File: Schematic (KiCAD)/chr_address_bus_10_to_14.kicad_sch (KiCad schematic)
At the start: 80 parts

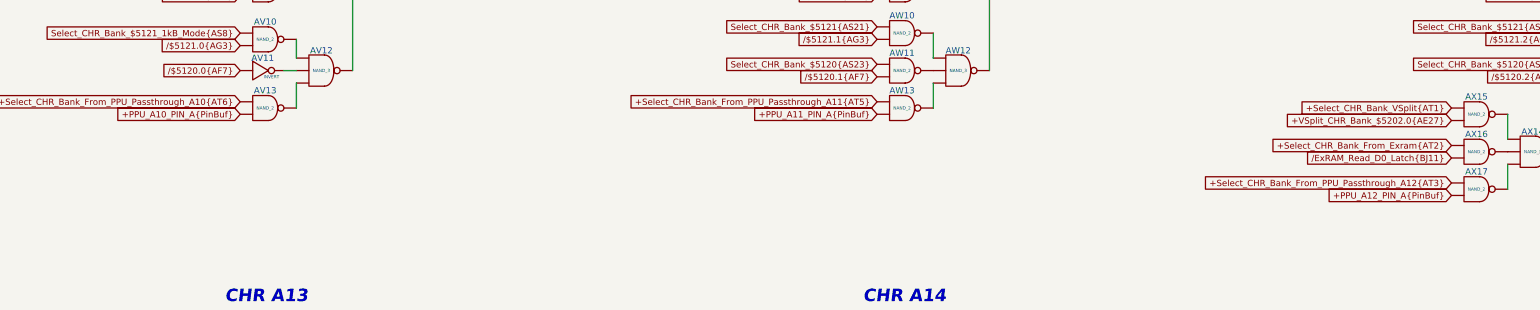
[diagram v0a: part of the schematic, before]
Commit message: Tracing and schematic updates.  - Added timer to schematic.  - Added all items from artifacts sheet to the MMC5A trace.
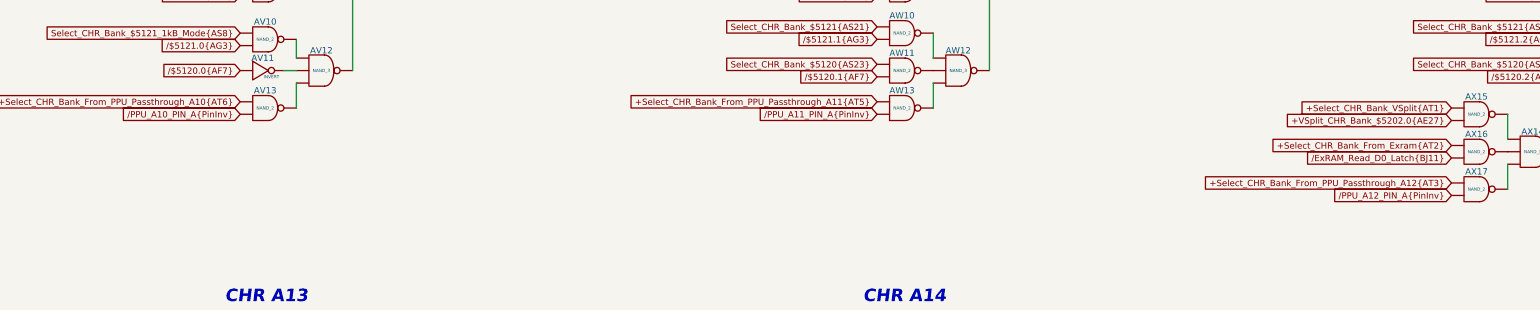
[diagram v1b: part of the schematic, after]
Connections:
- net +PPU_A10_PIN_A{PinBuf} is gone; now on net /PPU_A10_PIN_A{PinInv}: AV13. (X)
- net +PPU_A12_PIN_A{PinBuf} is gone; now on net /PPU_A12_PIN_A{PinInv}: AX17. (X)
- net at AX8. (X): now also AX6. (X); no longer AX7. (X)
- net at AV3. (X): now also AV4. (X); no longer AV1. (X)
- net at AW8. (X): now also AW6. (X); no longer AW5. (X)
- net at AW12. (X): now also AW11. (X); no longer AW13. (X)
- net at AX4. (X): now also AX2. (X); no longer AX9. (X)
- net at AZ14. (X): now also AZ13. (X); no longer AZ16. (X)
- net at AW9. (X): now also AW8. (X); no longer AW14. (X)
- net at AY8. (X): now also AY6. (X); no longer AY7. (X)
- net at AZ8. (X): now also AZ6. (X); no longer AZ5. (X)
- net at AY14. (X): now also AY13. (X); no longer AY15. (X)
- net at AY13. (X): now also AY12. (X); no longer AY14. (X)
- net at AX14. (X): now also AX17. (X); no longer AX16. (X)
- net at AX13. (X): now also AX12. (X); no longer AX14. (X)
- net /PPU_A12_PIN_A{PinInv}: now reaches AX17. (X)
- net /PPU_A12_PIN_A{PinInv}: no longer AX14. (X)
- net at AV9. (X): now also AV3. (X); no longer AV12. (X)
- net at AV8. (X): now also AV6. (X); no longer AV9. (X)
- net at AX12. (X): now also AX10. (X); no longer AX11. (X)
- net at AZ13. (X): now also AZ12. (X); no longer AZ14. (X)
- net at AX9. (X): now also AX18. (X); no longer AX12. (X)
- net at AY4. (X): now also AY9. (X); no longer AY1. (X)
- net at AZ4. (X): now also AZ2. (X); no longer AZ3. (X)
- net at AZ9. (X): now also AZ17. (X); no longer AZ4. (X)
- net at AY9. (X): now also AY17. (X); no longer AY4. (X)
- net at AV12. (X): now also AV13. (X); no longer AV10. (X)
- net /PPU_A10_PIN_A{PinInv}: now reaches AV13. (X)
- net /PPU_A10_PIN_A{PinInv}: no longer AV12. (X)
- net at AW4. (X): now also AW1. (X); no longer AW9. (X)
- net +PPU_A11_PIN_A{PinBuf} renamed /PPU_A11_PIN_A{PinInv}
- new net: AX7. (X), AX8. (X)
- new net: AV1. (X), AV3. (X)
- new net: AW5. (X), AW8. (X)
- new net: AW12. (X), AW13. (X)
- new net: AX4. (X), AX9. (X)
- new net: AX3. (X), AX4. (X)
- new net: AX1. (X), AX4. (X)
- new net: AZ14. (X), AZ16. (X)
- new net: AW14. (X), AW9. (X)
- new net: AY7. (X), AY8. (X)
- new net: AZ5. (X), AZ8. (X)
- new net: AW7. (X), AW8. (X)
- new net: AX5. (X), AX8. (X)
- new net: AY14. (X), AY15. (X)
- new net: AY14. (X), AY16. (X)
- new net: AX14. (X), AX16. (X)
- new net: AX13. (X), AX14. (X)
- new net: AX14. (X), AX15. (X)
- new net: AZ7. (X), AZ8. (X)
- new net: AV12. (X), AV9. (X)
- new net: AV8. (X), AV9. (X)
- new net: AV14. (X), AV9. (X)
- new net: AX11. (X), AX12. (X)
- new net: AZ14. (X), AZ15. (X)
- new net: AZ11. (X), AZ12. (X)
- new net: AX12. (X), AX9. (X)
- new net: AY1. (X), AY4. (X)
- new net: AZ3. (X), AZ4. (X)
- new net: AZ4. (X), AZ9. (X)
- new net: AZ1. (X), AZ4. (X)
- new net: AY3. (X), AY4. (X)
- new net: AY2. (X), AY4. (X)
- new net: AV10. (X), AV12. (X)
- new net: AV11. (X), AV12. (X)
- new net: AW12. (X), AW9. (X)
- new net: AW4. (X), AW9. (X)
- new net: AW10. (X), AW12. (X)
- new net: AX8. (X), AX9. (X)
- new net: AV7. (X), AV8. (X)
- new net: AY8. (X), AY9. (X)
- new net: AY5. (X), AY8. (X)
- new net: AV5. (X), AV8. (X)
- new net: AV2. (X), AV3. (X)
- new net: AY10. (X), AY12. (X)
- new net: AZ10. (X), AZ12. (X)
- new net: AW2. (X), AW4. (X)
- new net: AW3. (X), AW4. (X)
- new net: AZ12. (X), AZ9. (X)
- new net: AZ8. (X), AZ9. (X)
- new net: AY12. (X), AY9. (X)
- new net: AY11. (X), AY12. (X)
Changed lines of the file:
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@@
 		)
 	)
-	(global_label "+PPU_A10_PIN_A{PinBuf}"
+	(global_label "{slash}PPU_A10_PIN_A{PinInv}"
 		(shape input)
 		(at 74.93 97.79 180)
@@
 		)
 		(property "Intersheetrefs" "${INTERSHEET_REFS}"
-			(at 47.9357 97.79 0)
+			(at 48.6009 97.79 0)
 			(effects
 				(font
@@
 		)
 	)
-	(global_label "+PPU_A11_PIN_A{PinBuf}"
+	(global_label "{slash}PPU_A11_PIN_A{PinInv}"
 		(shape input)
 		(at 204.47 97.79 180)
@@
 		)
 		(property "Intersheetrefs" "${INTERSHEET_REFS}"
-			(at 177.4757 97.79 0)
+			(at 178.1409 97.79 0)
 			(effects
 				(font
@@
 		)
 	)
-	(global_label "+PPU_A12_PIN_A{PinBuf}"
+	(global_label "{slash}PPU_A12_PIN_A{PinInv}"
 		(shape input)
 		(at 321.31 114.3 180)
@@
 		)
 		(property "Intersheetrefs" "${INTERSHEET_REFS}"
-			(at 294.3157 114.3 0)
-			(effects
-				(font
+			(at 294.9809 114.3 0)
+			(effects
+				(font

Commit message: - Updated all of the various And-OR-Invert gates to have consistent names.  - Added the schematic for CL3 / SL3 GPIO pins.  There are no surprises revealed by this.  - Finished up the CPU address decoding tracing.  - Added one of the 'artifact' counters from the pulse channels
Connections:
- net at AX8. (X): now also AX6. (X); no longer AX7. (X)
- net at AV3. (X): now also AV4. (X); no longer AV1. (X)
- net at AW8. (X): now also AW6. (X); no longer AW5. (X)
- net at AW12. (X): now also AW11. (X); no longer AW13. (X)
- net at AX4. (X): now also AX2. (X); no longer AX9. (X)
- net at AZ14. (X): now also AZ13. (X); no longer AZ16. (X)
- net at AW9. (X): now also AW8. (X); no longer AW14. (X)
- net at AY8. (X): now also AY6. (X); no longer AY7. (X)
- net at AZ8. (X): now also AZ6. (X); no longer AZ5. (X)
- net at AY14. (X): now also AY13. (X); no longer AY15. (X)
- net at AY13. (X): now also AY12. (X); no longer AY14. (X)
- net at AX14. (X): now also AX17. (X); no longer AX16. (X)
- net at AX13. (X): now also AX12. (X); no longer AX14. (X)
- net at AV9. (X): now also AV3. (X); no longer AV12. (X)
- net at AV8. (X): now also AV6. (X); no longer AV9. (X)
- net at AX12. (X): now also AX10. (X); no longer AX11. (X)
- net at AZ13. (X): now also AZ12. (X); no longer AZ14. (X)
- net at AX9. (X): now also AX18. (X); no longer AX12. (X)
- net at AY4. (X): now also AY9. (X); no longer AY1. (X)
- net at AZ4. (X): now also AZ2. (X); no longer AZ3. (X)
- net at AZ9. (X): now also AZ17. (X); no longer AZ4. (X)
- net at AY9. (X): now also AY17. (X); no longer AY4. (X)
- net at AV12. (X): now also AV13. (X); no longer AV10. (X)
- net at AW4. (X): now also AW1. (X); no longer AW9. (X)
- new net: AX7. (X), AX8. (X)
- new net: AV1. (X), AV3. (X)
- new net: AW5. (X), AW8. (X)
- new net: AW12. (X), AW13. (X)
- new net: AX4. (X), AX9. (X)
- new net: AX3. (X), AX4. (X)
- new net: AX1. (X), AX4. (X)
- new net: AZ14. (X), AZ16. (X)
- new net: AW14. (X), AW9. (X)
- new net: AY7. (X), AY8. (X)
- new net: AZ5. (X), AZ8. (X)
- new net: AW7. (X), AW8. (X)
- new net: AX5. (X), AX8. (X)
- new net: AY14. (X), AY15. (X)
- new net: AY14. (X), AY16. (X)
- new net: AX14. (X), AX16. (X)
- new net: AX13. (X), AX14. (X)
- new net: AX14. (X), AX15. (X)
- new net: AZ7. (X), AZ8. (X)
- new net: AV12. (X), AV9. (X)
- new net: AV8. (X), AV9. (X)
- new net: AV14. (X), AV9. (X)
- new net: AX11. (X), AX12. (X)
- new net: AZ14. (X), AZ15. (X)
- new net: AZ11. (X), AZ12. (X)
- new net: AX12. (X), AX9. (X)
- new net: AY1. (X), AY4. (X)
- new net: AZ3. (X), AZ4. (X)
- new net: AZ4. (X), AZ9. (X)
- new net: AZ1. (X), AZ4. (X)
- new net: AY3. (X), AY4. (X)
- new net: AY2. (X), AY4. (X)
- new net: AV10. (X), AV12. (X)
- new net: AV11. (X), AV12. (X)
- new net: AW12. (X), AW9. (X)
- new net: AW4. (X), AW9. (X)
- new net: AW10. (X), AW12. (X)
- new net: AX8. (X), AX9. (X)
- new net: AV7. (X), AV8. (X)
- new net: AY8. (X), AY9. (X)
- new net: AY5. (X), AY8. (X)
- new net: AV5. (X), AV8. (X)
- new net: AV2. (X), AV3. (X)
- new net: AY10. (X), AY12. (X)
- new net: AZ10. (X), AZ12. (X)
- new net: AW2. (X), AW4. (X)
- new net: AW3. (X), AW4. (X)
- new net: AZ12. (X), AZ9. (X)
- new net: AZ8. (X), AZ9. (X)
- new net: AY12. (X), AY9. (X)
- new net: AY11. (X), AY12. (X)
